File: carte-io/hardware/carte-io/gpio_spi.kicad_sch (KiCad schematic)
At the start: 27 parts, among them J20 Conn_02x08_Odd_Even, J22 JST_PH_B6B, J23 JST_PH_B6B, J24 JST_PH_B6B, U22 CM1293A-04SO, U23 74LVC125APW, U24 CM1293A-04SO, U25 74LVC125APW, U30 74LVC125, U31 CM1293A-04SO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

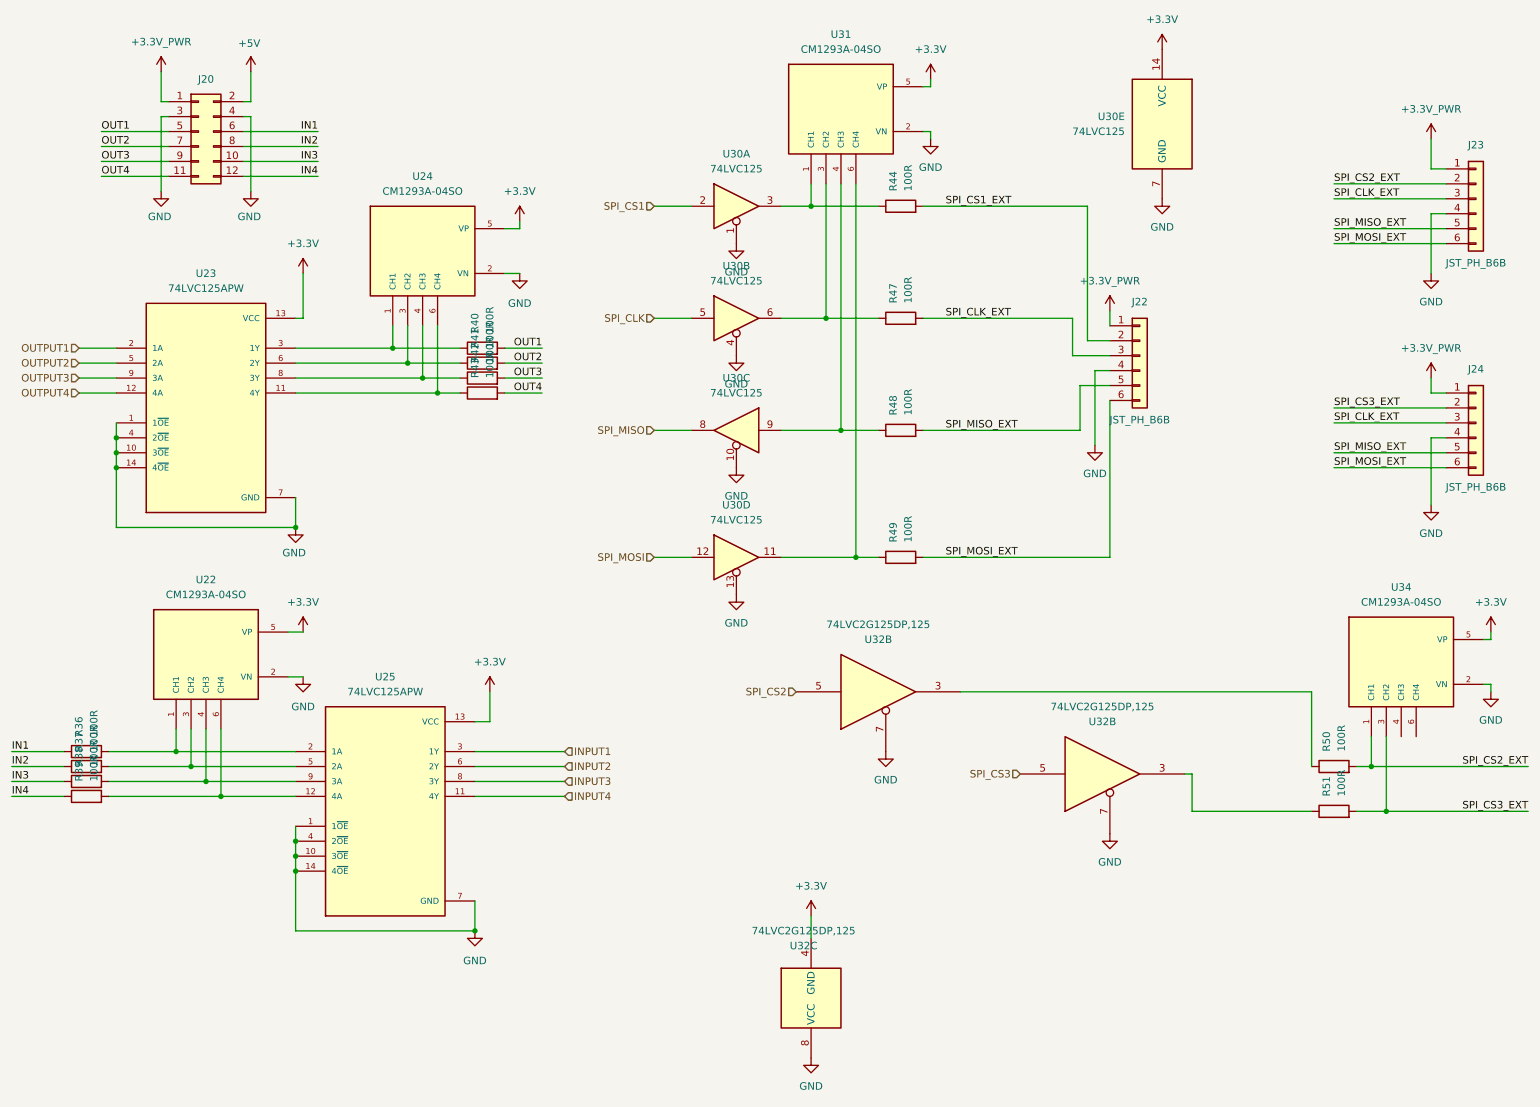
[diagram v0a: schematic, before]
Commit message: Carte IO routée version 1
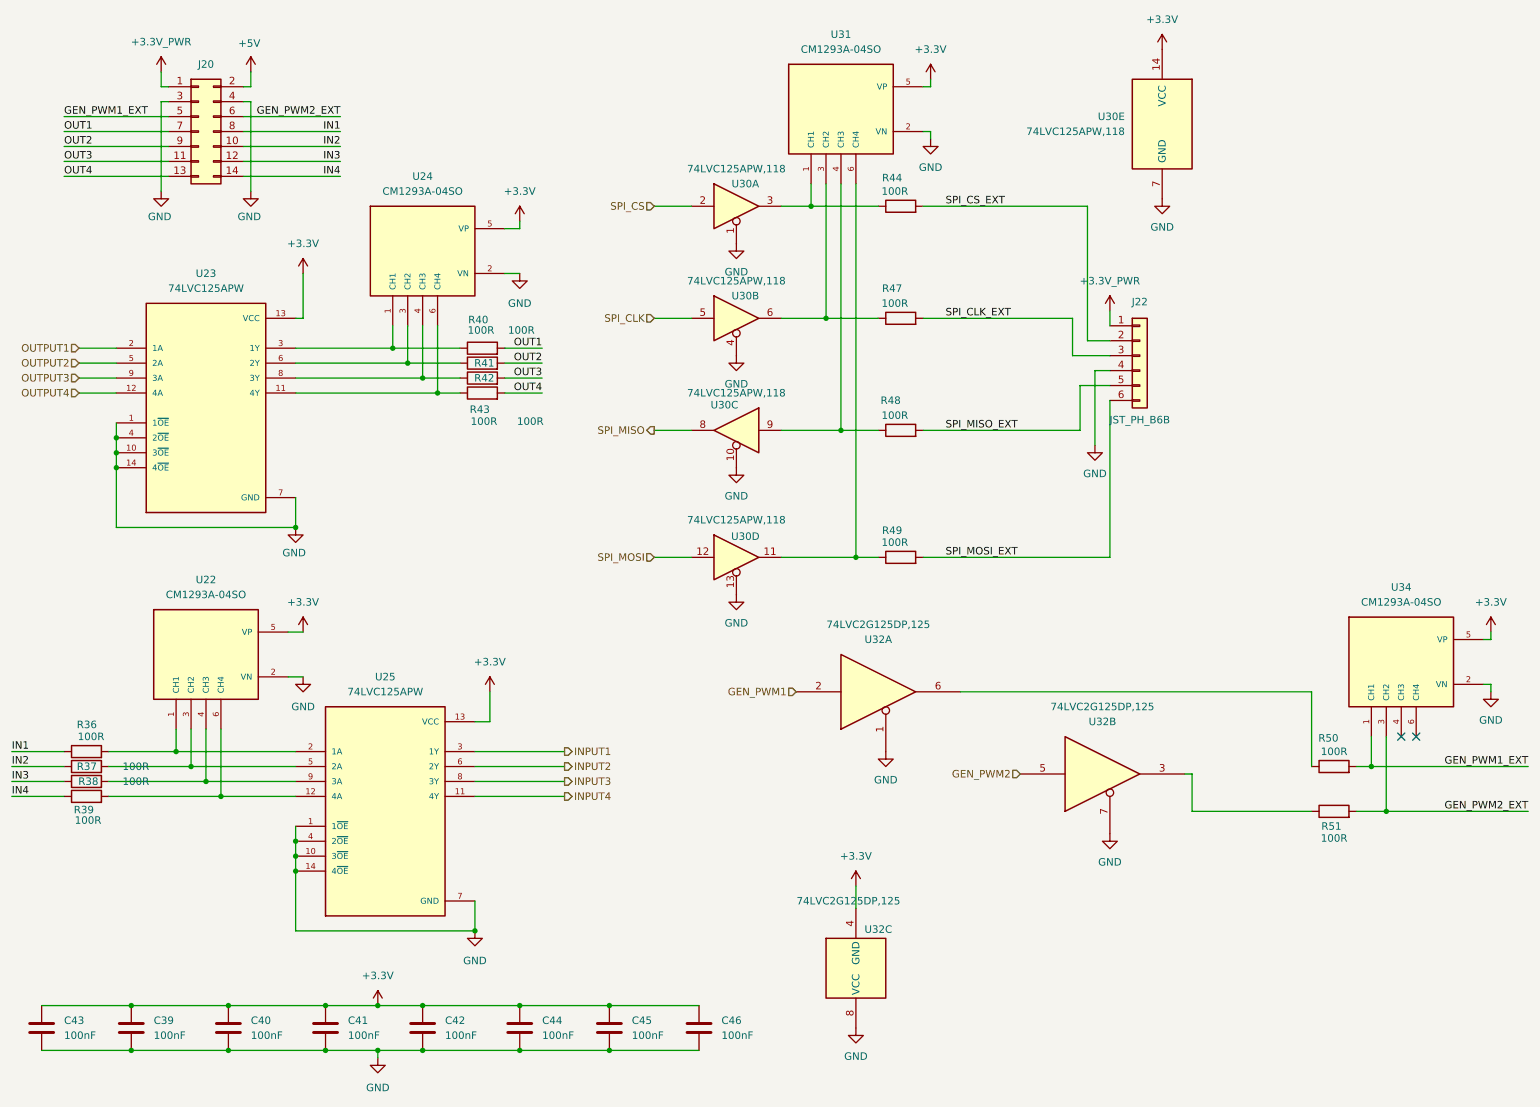
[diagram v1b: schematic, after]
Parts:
- removed J23, J24: JST_PH_B6B, Connector_JST:JST_PH_B6B-PH-K_1x06_P2.00mm_Vertical, symbol Connector_Generic:Conn_01x06
- removed U32: 74LVC2G125DP,125, Package_SO:VSSOP-8_2.3x2mm_P0.5mm, symbol 74xGxx:74LVC2G125
- added C39, C40, C41, C42, C43, C44, C45, C46: 100nF, Capacitor_SMD:C_0805_2012Metric_Pad1.18x1.45mm_HandSolder, symbol Device:C
- added unit 1 of U32
- J20: footprint Connector_PinHeader_2.54mm:PinHeader_2x06_P2.54mm_Vertical -> Connector_PinHeader_2.54mm:PinHeader_2x07_P2.54mm_Vertical; symbol Connector_Generic:Conn_02x06_Odd_Even -> Connector_Generic:Conn_02x07_Odd_Even
- U30: value 74LVC125 -> 74LVC125APW,118; footprint (none) -> Package_SO:TSSOP-14_4.4x5mm_P0.65mm
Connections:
- net +3.3V: now also C39.1, C40.1, C41.1, C42.1, C43.1, C44.1, C45.1, C46.1
- net GND: now also C39.2, C40.2, C41.2, C42.2, C43.2, C44.2, C45.2, C46.2, U32.1
- net IN1: now also J20.8 (Pin_8); no longer J20.6 (Pin_6)
- net IN2: now also J20.10 (Pin_10); no longer J20.8 (Pin_8)
- net IN3: now also J20.12 (Pin_12); no longer J20.10 (Pin_10)
- net IN4: now also J20.14 (Pin_14); no longer J20.12 (Pin_12)
- net OUT1: now also J20.7 (Pin_7); no longer J20.5 (Pin_5)
- net OUT2: now also J20.9 (Pin_9); no longer J20.7 (Pin_7)
- net OUT3: now also J20.11 (Pin_11); no longer J20.9 (Pin_9)
- net OUT4: now also J20.13 (Pin_13); no longer J20.11 (Pin_11)
- net at R50.1: now also U32.6
- net SPI_CS1 renamed SPI_CS
- net SPI_CS1_EXT renamed SPI_CS_EXT
- net SPI_CS2_EXT renamed GEN_PWM1_EXT
- net GEN_PWM1_EXT: now also J20.5 (Pin_5)
- net SPI_CS3 renamed GEN_PWM2
- net SPI_CS3_EXT renamed GEN_PWM2_EXT
- net GEN_PWM2_EXT: now also J20.6 (Pin_6)
- new net GEN_PWM1: U32.2
- no-connect marks 0 -> 2
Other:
- company: (none) -> INSA - GEI
- title: (none) -> GPIO & SPI
- moved on the sheet: U32C
